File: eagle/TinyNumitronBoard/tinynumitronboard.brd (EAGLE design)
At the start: 50 x 50 mm, 25 parts, among them IC1 74LS595N, IC2 74LS595N

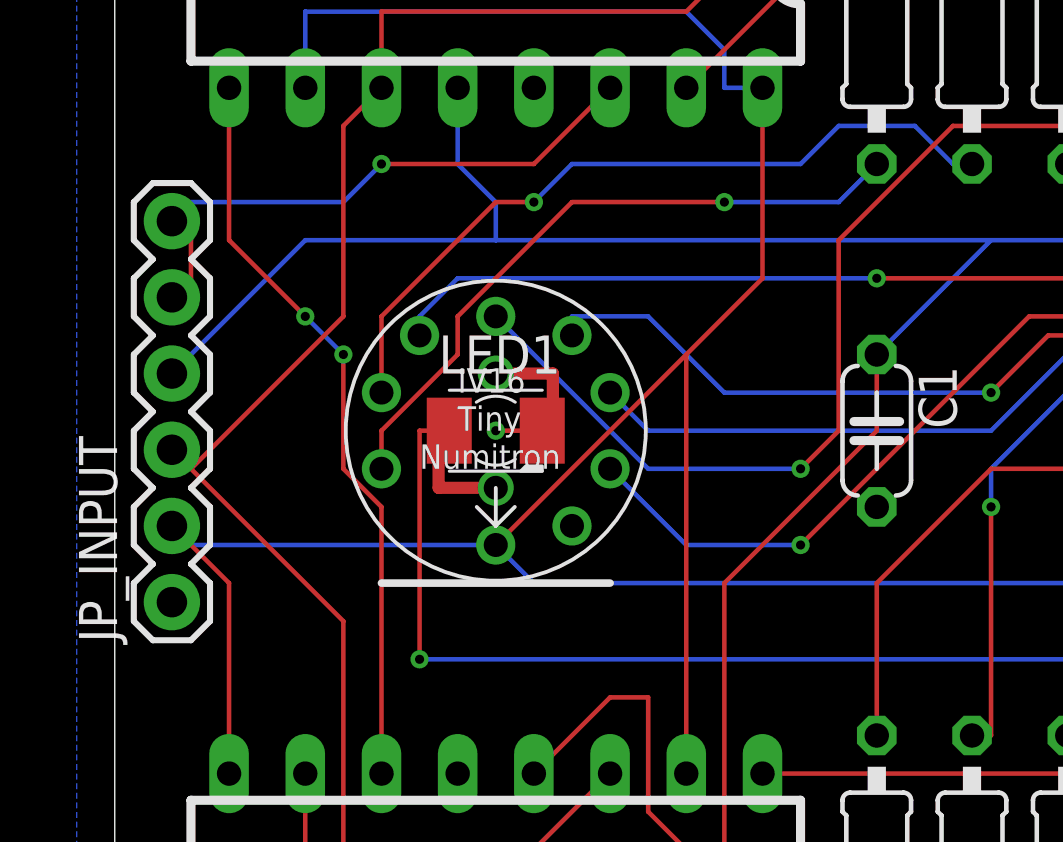
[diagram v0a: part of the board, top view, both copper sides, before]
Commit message: BUGFIX v1.1 : fixed unconnected central ground plane, fixed alignement of JP_IN / JP_OUT
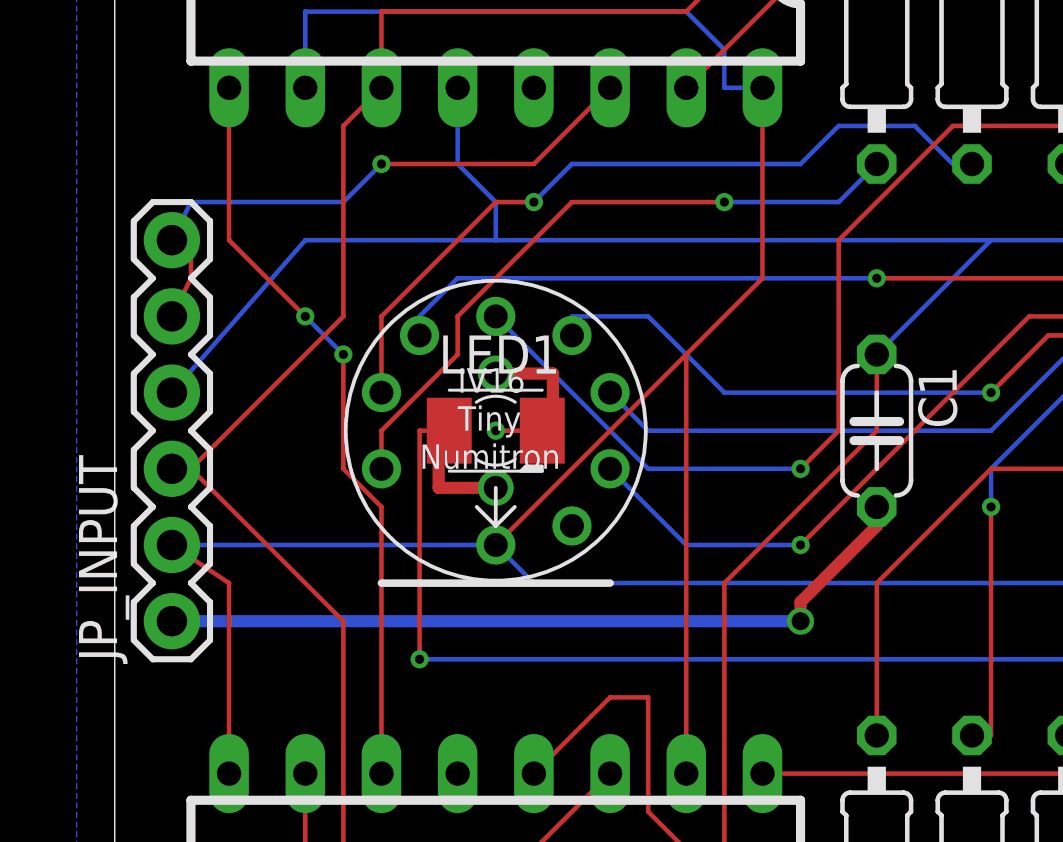
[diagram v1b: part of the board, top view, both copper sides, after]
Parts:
- moved JP_INPUT 0.63 mm to (1.91, 19.1)
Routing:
- net GND: track 3.18 -> 29.0 mm, vias 2 -> 3
- net N$15: track 19.5 -> 20.3 mm
- net VCC: track 110.2 -> 109.6 mm
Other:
- board text added: "+"
- board text added: "-"
- board text added: "Version 1.1 - Oct 2012"
- board text removed: "Version 1.0 - Sept 2012"
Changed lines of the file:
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@@
 <?xml version="1.0" encoding="utf-8"?>
 <!DOCTYPE eagle SYSTEM "eagle.dtd">
-<eagle version="6.0">
+<eagle version="6.3">
 <drawing>
 <settings>
@@
 <text x="3.81" y="19.05" size="1.016" layer="125">&gt;GND</text>
 <text x="10.16" y="0.635" size="1.27" layer="125">http://kalshagar.wikispaces.com</text>
-<text x="13.335" y="1.905" size="1.27" layer="125">Version 1.0 - Sept 2012</text>
+<text x="13.335" y="1.905" size="1.27" layer="125">Version 1.1 - Oct 2012</text>
 <text x="5.08" y="48.26" size="1.27" layer="125">Order ########</text>
 <text x="48.26" y="38.1" size="1.016" layer="125" rot="R90">LED</text>
@@
 <text x="35.56" y="19.05" size="1.016" layer="125">RIGHT</text>
 <text x="10.795" y="19.05" size="1.016" layer="125">LEFT</text>
+<text x="14.605" y="26.035" size="1.27" layer="125" rot="R270">-</text>
+<text x="35.56" y="24.765" size="1.27" layer="125" rot="R90">-</text>
+<text x="40.005" y="24.765" size="1.27" layer="125">+</text>
+<text x="9.525" y="24.765" size="1.27" layer="125">+</text>
 </plain>
 <attributes>
@@
 </class>
 </classes>
-<designrules>
+<designrules name="default">
 <description language="de">&lt;b&gt;EAGLE Design Rules&lt;/b&gt;
 &lt;p&gt;
@@
 <element name="R7" library="resistor" package="0207/10" value="" x="44.45" y="39.37" rot="R270"/>
 <element name="IC2" library="SparkFun" package="DIL16" value="74LS595N" x="12.7" y="40.64" rot="R180"/>
-<element name="JP_INPUT" library="SparkFun" package="1X06" value="" x="1.905" y="19.685" rot="R90"/>
+<element name="JP_INPUT" library="SparkFun" package="1X06" value="" x="1.905" y="19.05" rot="R90"/>
 <element name="LED1" library="led" package="KA-3528ASYC" value="" x="12.7" y="25.4"/>
 <element name="R8" library="resistor" package="0207/10" value="" x="47.625" y="39.37" rot="R270"/>
@@
 <wire x1="38.1" y1="21.59" x2="37.465" y2="21.59" width="0.1524" layer="16"/>
 <wire x1="3.81" y1="20.32" x2="3.81" y2="13.97" width="0.1524" layer="1"/>
-<wire x1="1.905" y1="22.225" x2="3.81" y2="20.32" width="0.1524" layer="1"/>
+<wire x1="1.905" y1="21.59" x2="3.81" y2="20.32" width="0.1524" layer="1"/>
 <wire x1="21.59" y1="30.48" x2="19.05" y2="27.94" width="0.1524" layer="1"/>
 <wire x1="19.05" y1="27.94" x2="12.7" y2="21.59" width="0.1524" layer="1"/>
@@
 <wire x1="21.59" y1="36.83" x2="20.32" y2="36.83" width="0.1524" layer="16"/>
 <wire x1="19.05" y1="27.94" x2="19.05" y2="13.97" width="0.1524" layer="1"/>
-<wire x1="12.7" y1="21.59" x2="2.54" y2="21.59" width="0.1524" layer="16"/>
-<wire x1="2.54" y1="21.59" x2="1.905" y2="22.225" width="0.1524" layer="16"/>
+<wire x1="12.7" y1="21.59" x2="1.905" y2="21.59" width="0.1524" layer="16"/>
 <wire x1="35.56" y1="20.32" x2="36.83" y2="21.59" width="0.1524" layer="16"/>
 <wire x1="13.97" y1="20.32" x2="35.56" y2="20.32" width="0.1524" layer="16"/>
@@
 <via x="12.7" y="25.4" extent="1-16" drill="0.3048"/>
 <via x="34.29" y="25.4" extent="1-16" drill="0.3048"/>
-<wire x1="14.25" y1="25.4" x2="13.97" y2="36.83" width="0" layer="19" extent="1-1"/>
+<via x="22.86" y="19.05" extent="1-16" drill="0.6"/>
+<wire x1="1.905" y1="19.05" x2="22.86" y2="19.05" width="0.4064" layer="16"/>
+<wire x1="22.86" y1="19.05" x2="22.86" y2="19.685" width="0.4064" layer="1"/>
+<wire x1="22.86" y1="19.685" x2="25.4" y2="22.225" width="0.4064" layer="1"/>
+<wire x1="25.4" y1="22.225" x2="25.4" y2="22.86" width="0.4064" layer="1"/>
 </signal>
 <signal name="N$16">
@@
 <wire x1="7.62" y1="33.02" x2="8.89" y2="34.29" width="0.1524" layer="16"/>
 <wire x1="2.54" y1="33.02" x2="7.62" y2="33.02" width="0.1524" layer="16"/>
-<wire x1="2.54" y1="33.02" x2="1.905" y2="32.385" width="0.1524" layer="16"/>
+<wire x1="2.54" y1="33.02" x2="1.905" y2="31.75" width="0.1524" layer="16"/>
 <wire x1="2.54" y1="31.75" x2="2.54" y2="30.48" width="0.1524" layer="1"/>
-<wire x1="2.54" y1="30.48" x2="1.905" y2="29.845" width="0.1524" layer="1"/>
-<wire x1="2.54" y1="31.75" x2="1.905" y2="32.385" width="0.1524" layer="1"/>
+<wire x1="2.54" y1="30.48" x2="1.905" y2="29.21" width="0.1524" layer="1"/>
+<wire x1="2.54" y1="31.75" x2="1.905" y2="31.75" width="0.1524" layer="1"/>
 <via x="8.89" y="34.29" extent="1-16" drill="0.3048"/>
 </signal>
@@
 <wire x1="12.7" y1="31.75" x2="12.7" y2="33.02" width="0.1524" layer="16"/>
 <wire x1="6.35" y1="31.75" x2="12.7" y2="31.75" width="0.1524" layer="16"/>
-<wire x1="1.905" y1="27.305" x2="6.35" y2="31.75" width="0.1524" layer="16"/>
+<wire x1="1.905" y1="26.67" x2="6.35" y2="31.75" width="0.1524" layer="16"/>
 <wire x1="16.51" y1="16.51" x2="13.97" y2="13.97" width="0.1524" layer="1"/>
 <wire x1="17.78" y1="16.51" x2="16.51" y2="16.51" width="0.1524" layer="1"/>
@@
 <wire x1="7.62" y1="29.21" x2="7.62" y2="35.56" width="0.1524" layer="1"/>
 <wire x1="2.54" y1="24.13" x2="7.62" y2="29.21" width="0.1524" layer="1"/>
-<wire x1="2.54" y1="24.13" x2="1.905" y2="24.765" width="0.1524" layer="1"/>
+<wire x1="2.54" y1="24.13" x2="1.905" y2="24.13" width="0.1524" layer="1"/>
 <wire x1="44.45" y1="24.13" x2="48.26" y2="24.13" width="0.1524" layer="16"/>
 <wire x1="44.45" y1="33.02" x2="44.45" y2="24.13" width="0.1524" layer="1"/>

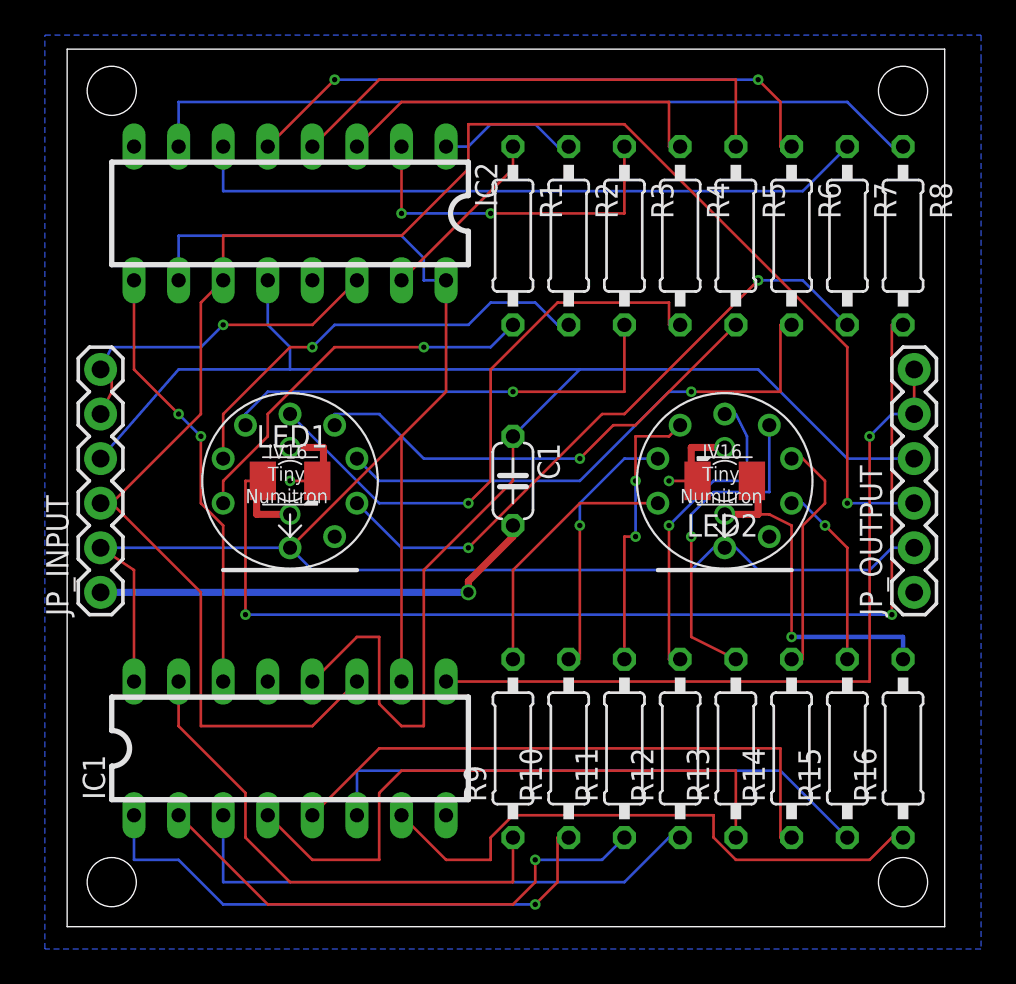
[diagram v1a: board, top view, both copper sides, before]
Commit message: Dual version that accepts also SO16 version of 74595
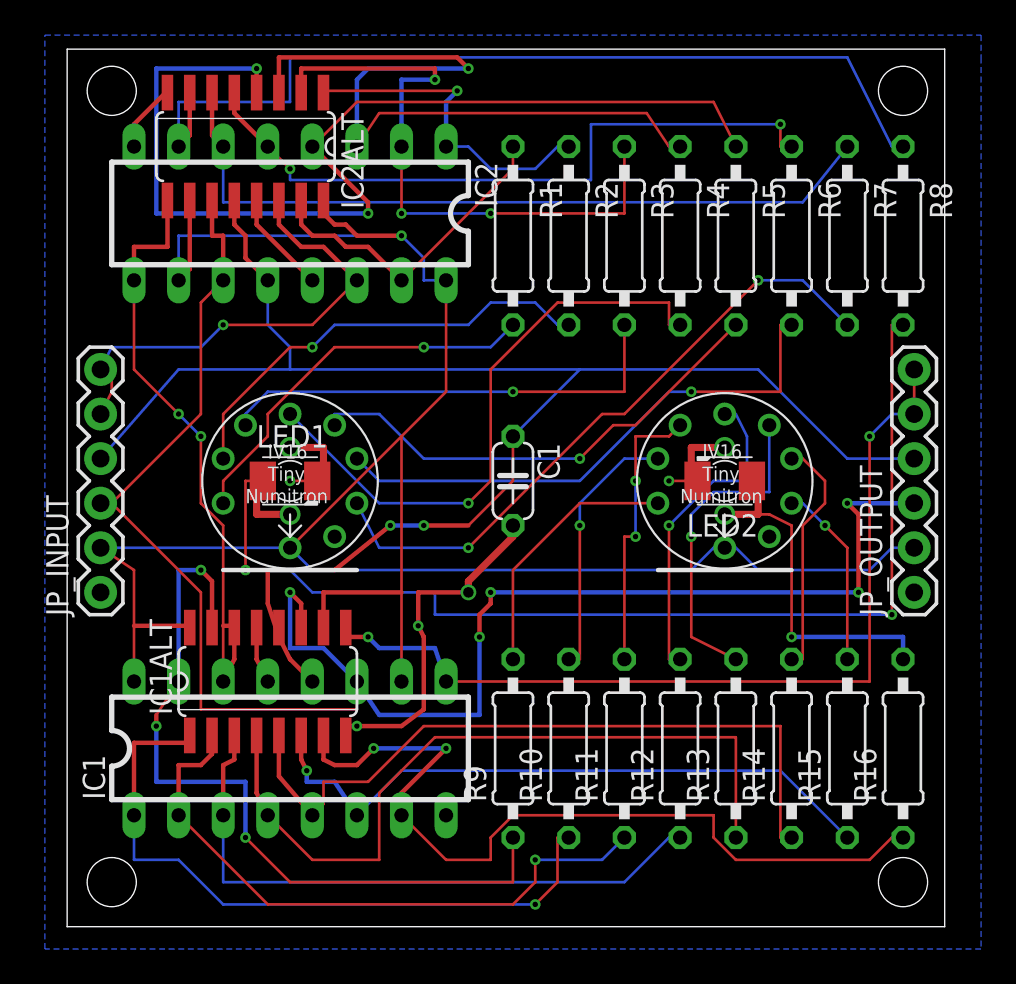
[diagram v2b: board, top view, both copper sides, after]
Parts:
- added IC1ALT, IC2ALT: 74HCT595D, 74xx-eu:SO16
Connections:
- removed net N$18: C1.1, IC1.12, IC2.12, JP_INPUT.4, JP_OUTPUT.4
- removed net N$29: IC1.15, R9.1
- removed net N$30: IC1.1, R10.1
- removed net N$31: IC1.2, R11.1
- removed net N$32: IC1.3, R12.1
- removed net N$33: IC1.4, R13.1
- removed net N$34: IC1.5, R14.1
- removed net N$35: IC1.6, R15.1
- removed net N$36: IC1.7, R16.1
- new net N$23: IC1.14, IC1ALT.14, IC2.9, IC2ALT.9
- new net N$39: IC2.1, IC2ALT.1, R2.1
- new net N$41: IC2.15, IC2ALT.15, R1.1
- new net N$42: IC2.6, IC2ALT.6, R7.1
- new net N$43: IC2.5, IC2ALT.5, R6.1
- new net N$48: C1.1, IC1.12, IC1ALT.12, IC2.12, IC2ALT.12, JP_INPUT.4, JP_OUTPUT.4
- new net N$52: IC1.15, IC1ALT.15, R9.1
- new net N$54: IC1.11, IC1ALT.11, IC2.11, IC2ALT.11, JP_INPUT.3, JP_OUTPUT.3
- new net N$56: IC1.9, IC1ALT.9, JP_OUTPUT.5, JP_OUTPUT.6
- net GND: now also IC1ALT.13, IC1ALT.8, IC2ALT.13, IC2ALT.8
- net N$10: now also IC1.3, IC1ALT.3, R12.1; no longer IC2.2, R3.1
- net N$11: now also IC1.4, IC1ALT.4, R13.1; no longer IC2.3, R4.1
- net N$12: now also IC2ALT.4
- net N$13: now also IC2.3, IC2ALT.3, R4.1; no longer IC2.5, R6.1
- net N$14: now also IC1.5, IC1ALT.5, R14.1; no longer IC2.6, R7.1
- net N$15: now also IC1.6, IC1ALT.6, R15.1; no longer IC2.14, JP_INPUT.5, JP_INPUT.6
- net N$16: now also IC2ALT.7
- net N$19: now also IC2.2, IC2ALT.2, R3.1; no longer IC1.11, IC2.11, JP_INPUT.3, JP_OUTPUT.3
- net N$22: now also IC1.7, IC1ALT.7, R16.1; no longer IC1.9, JP_OUTPUT.5, JP_OUTPUT.6
- net N$38: now also IC2.14, IC2ALT.14, JP_INPUT.5, JP_INPUT.6; no longer IC1.14, IC2.9
- net N$8: now also IC1.1, IC1ALT.1, R10.1; no longer IC2.15, R1.1
- net N$9: now also IC1.2, IC1ALT.2, R11.1; no longer IC2.1, R2.1
- net VCC: now also IC1ALT.10, IC1ALT.16, IC2ALT.10, IC2ALT.16
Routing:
- net N$54: track 0.00 -> 100.7 mm, vias 0 -> 5
- net N$48: track 0.00 -> 92.6 mm, vias 0 -> 2
- net N$18: track 92.1 -> 0.00 mm
- net N$19: track 100.9 -> 35.6 mm, vias 1 -> 3
- net N$56: track 0.00 -> 51.7 mm, vias 0 -> 2
- net N$52: track 0.00 -> 44.2 mm, vias 0 -> 3
- net N$42: track 0.00 -> 43.7 mm
- net N$43: track 0.00 -> 39.4 mm, vias 0 -> 2
- net N$33: track 35.9 -> 0.00 mm
- net N$23: track 0.00 -> 35.3 mm, vias 0 -> 2
- net N$34: track 34.0 -> 0.00 mm
- net N$36: track 33.7 -> 0.00 mm
- net N$35: track 32.1 -> 0.00 mm
- net N$30: track 31.4 -> 0.00 mm, vias 1 -> 0
- net N$32: track 30.9 -> 0.00 mm
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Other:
- board text removed: "Order ########"
